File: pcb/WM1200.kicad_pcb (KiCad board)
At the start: 4 copper layers, 159 x 104 mm, 133 parts, among them Q1 BC817, Q2 BC817, Q3 BC817, Q4 BC817, Q5 BC817, Q6 BC817, U1 74LVCH162245A, U2 74LVCH162245A, U3 74LVCH162245A, U4 74LVCH162245A, U5 74LVCH162245A, U6 ADP2108AUJ-3.3, U7 TPD12S016PWR, X1 audio_expansion, X2 A1200_trapdoor_connector, X4 AC7020, X5 Conn_02x05_Odd_Even, X6 HDMI_A

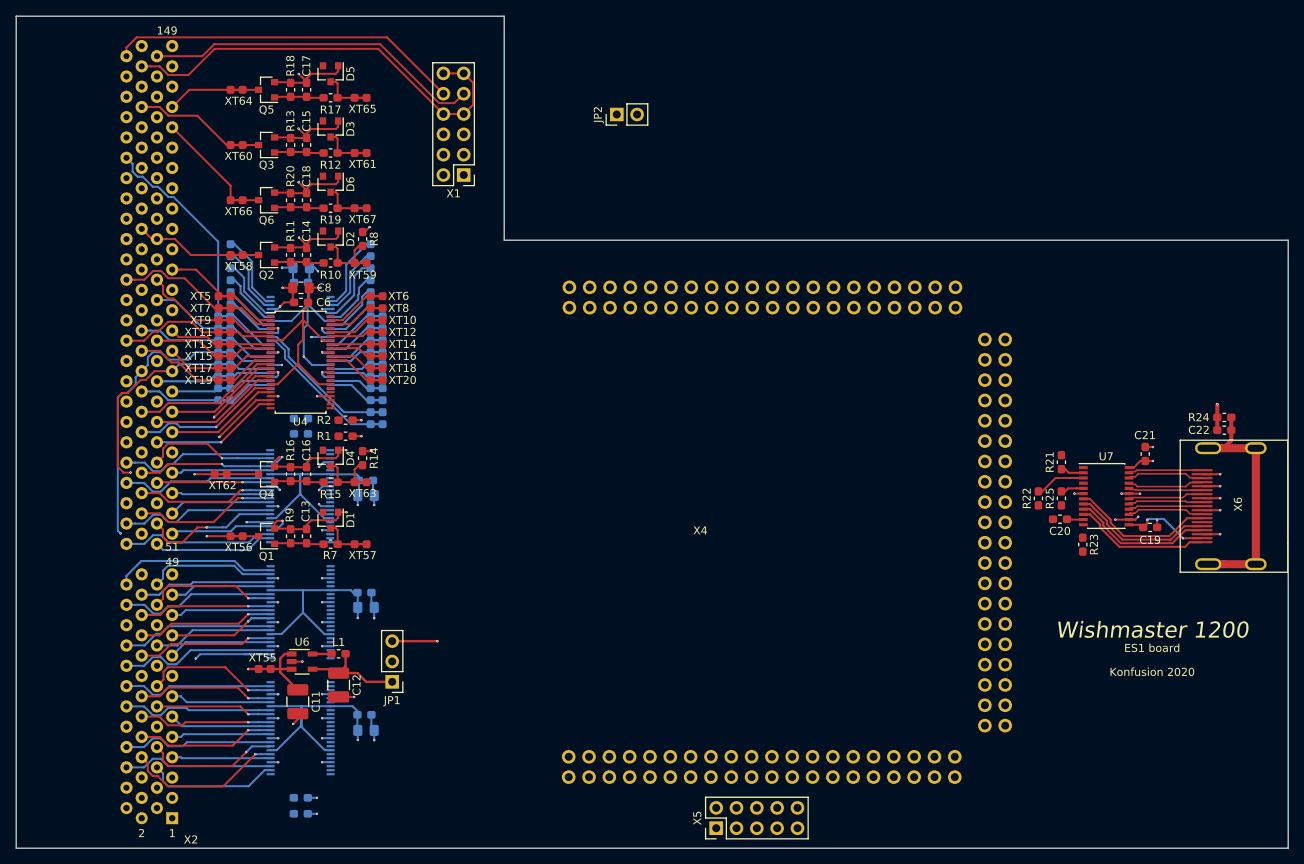
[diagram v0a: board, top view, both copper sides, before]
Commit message: Buffers power scheme rework in progress, re-annotate board
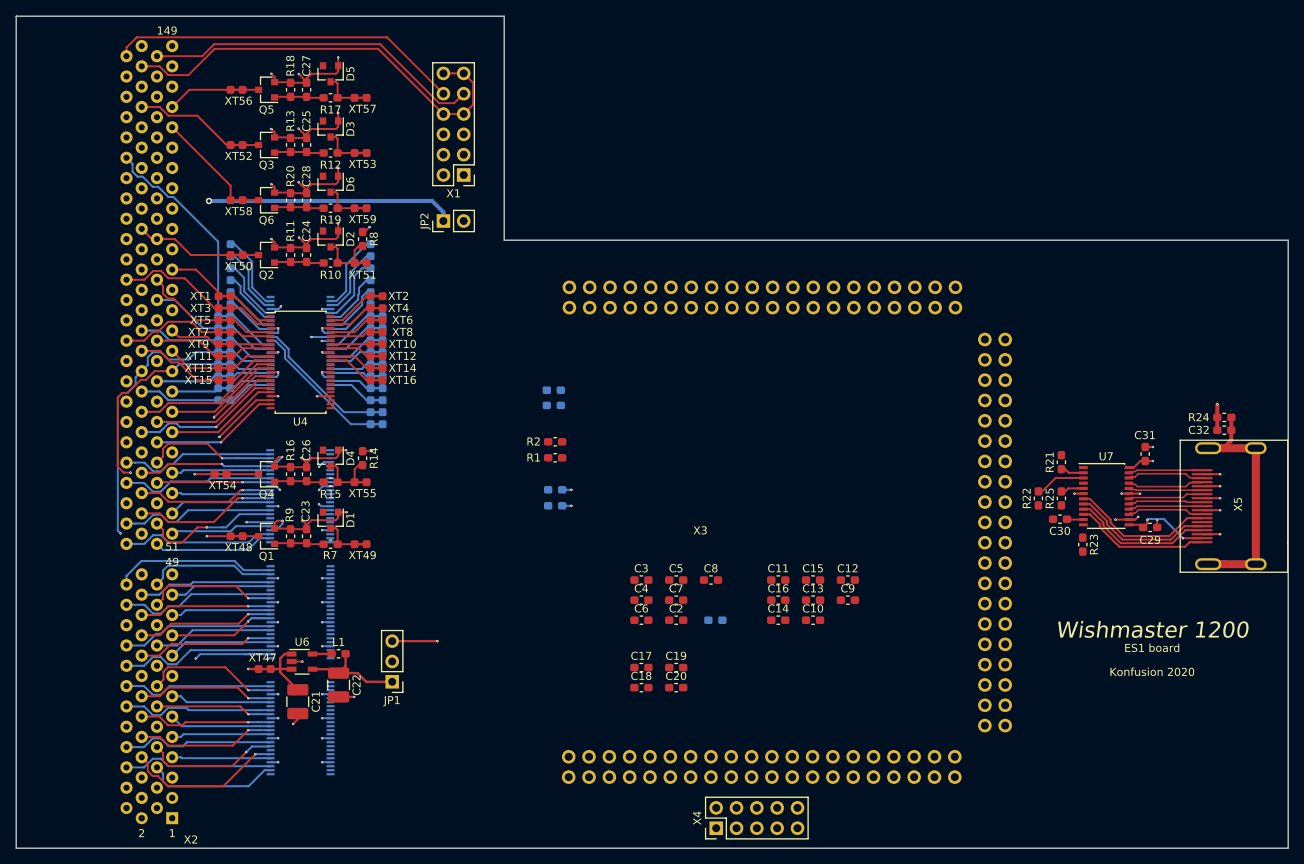
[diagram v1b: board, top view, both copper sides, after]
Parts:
- added C11: 0.1uF 35V, Capacitor_SMD:C_0603_1608Metric_Pad1.05x0.95mm_HandSolder, F.Cu at (185.3, 116.5)
- added C12: 0.1uF 35V, Capacitor_SMD:C_0603_1608Metric_Pad1.05x0.95mm_HandSolder, F.Cu at (194.0, 116.5)
- added C13: 0.1uF 35V, Capacitor_SMD:C_0603_1608Metric_Pad1.05x0.95mm_HandSolder, F.Cu at (189.6, 119.0)
- added C14: 0.1uF 35V, Capacitor_SMD:C_0603_1608Metric_Pad1.05x0.95mm_HandSolder, F.Cu at (185.3, 121.5)
- added C15: 0.1uF 35V, Capacitor_SMD:C_0603_1608Metric_Pad1.05x0.95mm_HandSolder, F.Cu at (189.6, 116.5)
- added C16: 0.1uF 35V, Capacitor_SMD:C_0603_1608Metric_Pad1.05x0.95mm_HandSolder, F.Cu at (185.3, 119.0)
- added C17: 0.1uF 35V, Capacitor_SMD:C_0603_1608Metric_Pad1.05x0.95mm_HandSolder, F.Cu at (168.2, 127.4)
- added C18: 0.1uF 35V, Capacitor_SMD:C_0603_1608Metric_Pad1.05x0.95mm_HandSolder, F.Cu at (168.2, 129.9)
- added C19: 0.1uF 35V, Capacitor_SMD:C_0603_1608Metric_Pad1.05x0.95mm_HandSolder, F.Cu at (172.5, 127.4)
- added C20: 0.1uF 35V, Capacitor_SMD:C_0603_1608Metric_Pad1.05x0.95mm_HandSolder, F.Cu at (172.5, 129.9)
- C10, C3, C4, C7: value 1uF 35V -> 0.1uF 35V; footprint Capacitor_SMD:C_0805_2012Metric_Pad1.15x1.40mm_HandSolder -> Capacitor_SMD:C_0603_1608Metric_Pad1.05x0.95mm_HandSolder; moved to F.Cu
- C2, C5, C9: moved to F.Cu
- C8: value 1uF 35V -> 0.1uF 35V; footprint Capacitor_SMD:C_0805_2012Metric_Pad1.15x1.40mm_HandSolder -> Capacitor_SMD:C_0603_1608Metric_Pad1.05x0.95mm_HandSolder
- moved C9 79.1 mm to (194.0, 119.0)
- moved C10 77.7 mm to (189.6, 121.5)
- moved C8 62.9 mm to (176.8, 116.5)
- moved C6 58.2 mm to (168.2, 121.5)
- moved R3 49.9 mm to (157.4, 105.2)
- moved R4 49.9 mm to (157.4, 107.2)
- moved C1 44.0 mm to (177.4, 121.5)
- moved C2 42.5 mm to (172.5, 121.5), turned to 0 degrees
- moved C5 42.5 mm to (172.5, 116.5), turned to 0 degrees
- moved C7 42.1 mm to (172.5, 119.0), turned to 0 degrees
- moved C4 36.8 mm to (168.2, 119.0), turned to 0 degrees
- moved C3 34.6 mm to (168.2, 116.5), turned to 0 degrees
- moved R5 31.8 mm to (157.2, 92.8)
- moved R6 31.8 mm to (157.2, 94.7)
- moved R1 26.3 mm to (157.4, 101.2)
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- renumbered C11 to C21, C12 to C22, C13 to C23, C14 to C24, C15 to C25, C16 to C26, C17 to C27, C18 to C28, C19 to C29, C20 to C30, C21 to C31, C22 to C32, X4 to X3, X5 to X4, X6 to X5, XT5 to XT1, XT14 to XT10, XT15 to XT11, XT16 to XT12, XT17 to XT13, XT18 to XT14, XT19 to XT15, XT20 to XT16, XT37 to XT17, XT38 to XT18, XT39 to XT19, XT6 to XT2, XT40 to XT20, XT41 to XT21, XT42 to XT22, XT43 to XT23, XT44 to XT24, XT45 to XT25, XT46 to XT26, XT47 to XT27, XT48 to XT28, XT49 to XT29, XT7 to XT3, XT50 to XT30, XT51 to XT31, XT52 to XT32, XT21 to XT33, XT23 to XT34, XT24 to XT35, XT26 to XT36, XT27 to XT37, XT28 to XT38, XT29 to XT39, XT8 to XT4, XT30 to XT40, XT31 to XT41, XT32 to XT42, XT33 to XT43, XT34 to XT44, XT35 to XT45, XT36 to XT46, XT55 to XT47, XT56 to XT48, XT57 to XT49, XT9 to XT5, XT58 to XT50, XT59 to XT51, XT60 to XT52, XT61 to XT53, XT62 to XT54, XT63 to XT55, XT64 to XT56, XT65 to XT57, XT66 to XT58, XT67 to XT59, XT10 to XT6, XT11 to XT7, XT12 to XT8, XT13 to XT9
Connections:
- X3 pad J10_26: FPGA_A_BUFF_DIR -> Net-(X3-PadJ10_26)
- X3 pad J10_28: _FPGA_A_BUFF_OE -> Net-(X3-PadJ10_28)
- X3 pad J12_34: FPGA_D_BUFF_DIR -> Net-(X3-PadJ12_34)
- X3 pad J12_36: _FPGA_D_BUFF_OE -> Net-(X3-PadJ12_36)
- XT33 pad 1: _FPGA_DSACK1 -> Net-(XT33-Pad1)
- XT34 pad 1: _FPGA_DSACK0 -> Net-(XT34-Pad1)
- XT49 pad 1: FPGA_OC_HLT -> Net-(XT49-Pad1)
- XT51 pad 1: FPGA_OC_BOSS -> Net-(XT51-Pad1)
- XT53 pad 1: FPGA_OC_INT6 -> Net-(XT53-Pad1)
- XT55 pad 1: FPGA_OC_RST -> Net-(XT55-Pad1)
- XT57 pad 1: FPGA_OC_INT2 -> Net-(XT57-Pad1)
- XT59 pad 1: FPGA_OC_OVR -> Net-(XT59-Pad1)
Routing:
- net +3V3_BUFFER: track 151.7 -> 3.46 mm, vias 11 -> 3
- net +5VDC: track 5.12 -> 36.1 mm, vias 1 -> 2
- net GND: track 164.9 -> 156.3 mm, vias 63 -> 67

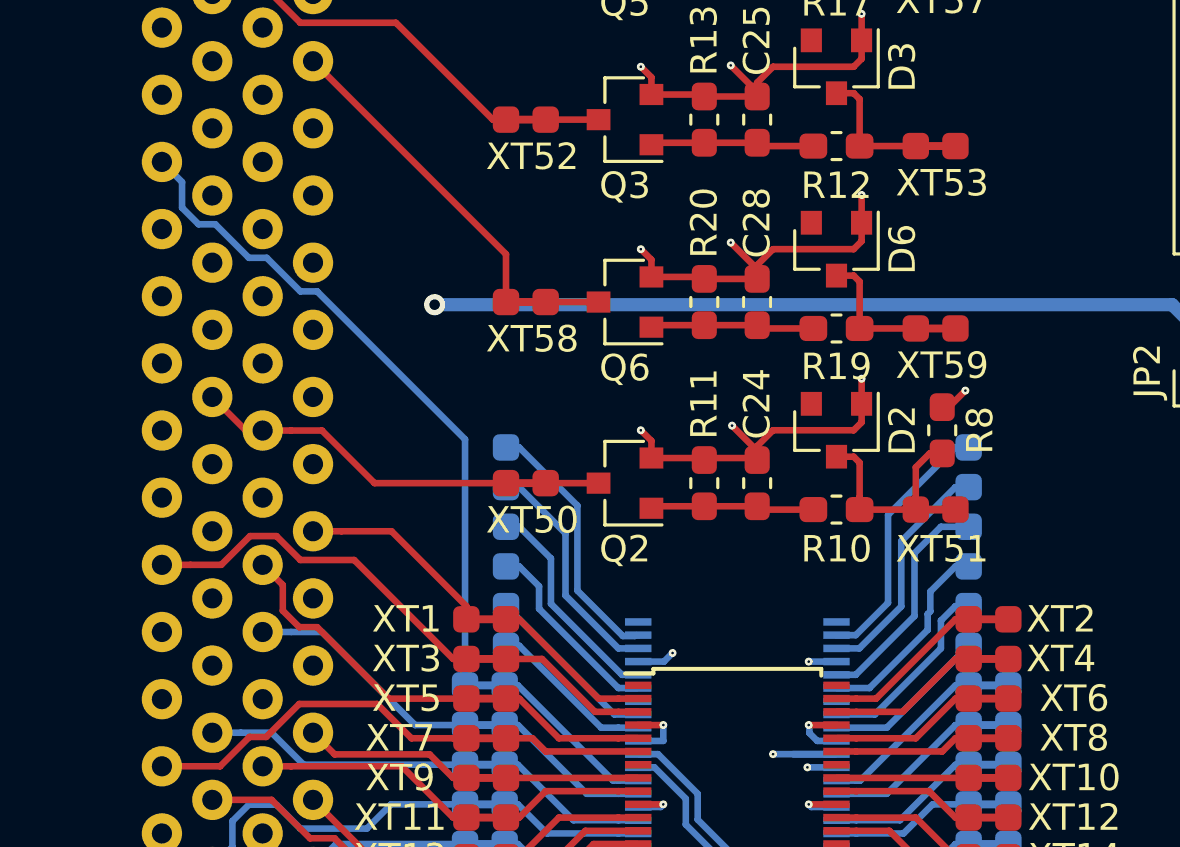
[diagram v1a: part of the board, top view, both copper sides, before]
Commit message: Unused buffer io are now grounded via testpads
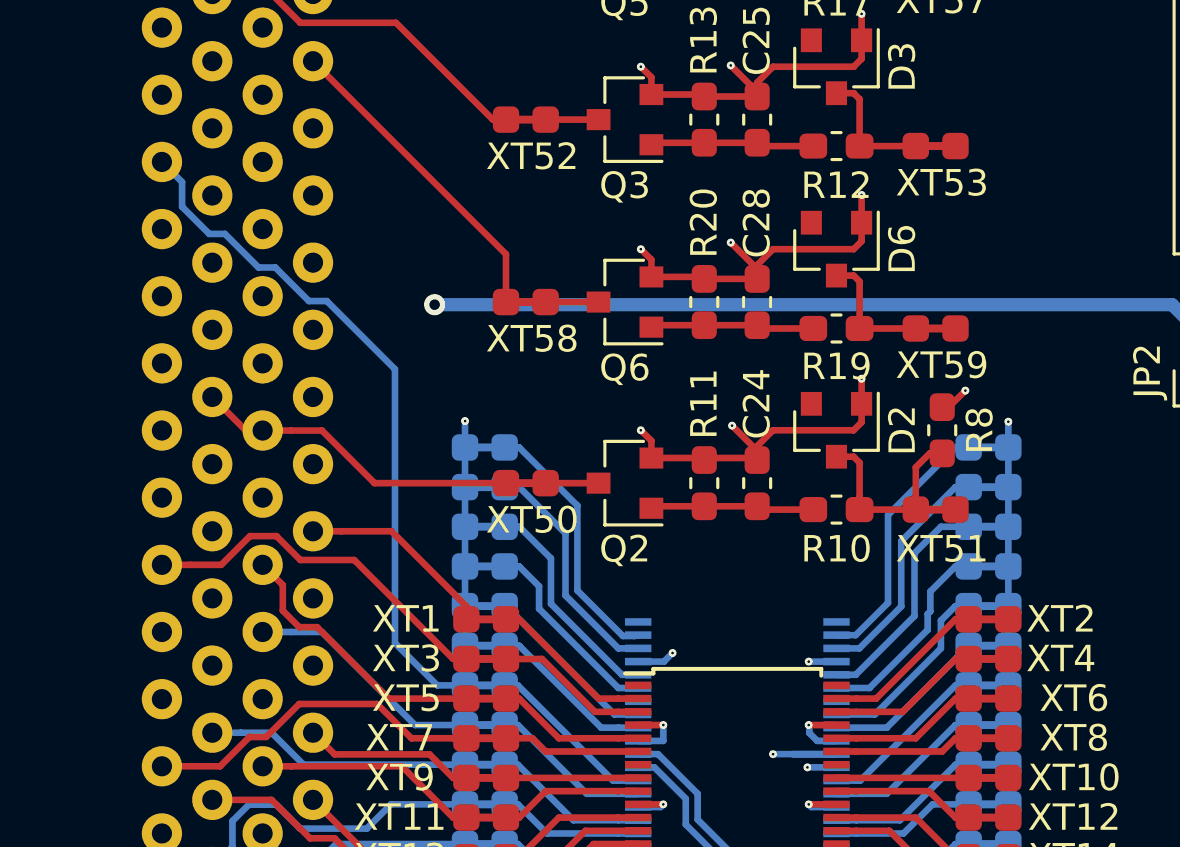
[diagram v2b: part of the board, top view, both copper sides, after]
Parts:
- XT35, XT36, XT37, XT38, XT39, XT40, XT41, XT42, XT43, XT44, XT45, XT46: value testpoint -> testpoint_cutline; footprint WM1200:testpoint -> WM1200:testpoint_cutline
- moved XT37 18.6 mm to (115.8, 82.4)
- moved XT39 18.6 mm to (115.8, 80.9)
- moved XT41 18.6 mm to (115.8, 79.4)
- moved XT43 18.6 mm to (115.8, 77.9)
- moved XT45 18.6 mm to (115.8, 76.4)
- moved XT36 18.3 mm to (134.8, 83.9)
- moved XT38 18.3 mm to (134.8, 82.4)
- moved XT40 18.3 mm to (134.8, 80.9)
- moved XT42 18.3 mm to (134.8, 79.4)
- moved XT44 18.3 mm to (134.8, 77.9), turned to 0 degrees
- moved XT35 2.18 mm to (115.8, 83.9)
- moved XT46 1.97 mm to (134.8, 76.4)
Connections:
- XT35 pad 1: Net-(U5-Pad16) -> GND
- XT36 pad 1: Net-(U5-Pad17) -> Net-(U5-Pad33)
- XT37 pad 1: Net-(U5-Pad33) -> GND
- XT38 pad 1: Net-(U5-Pad19) -> Net-(U5-Pad32)
- XT39 pad 1: Net-(U5-Pad32) -> GND
- XT40 pad 1: Net-(U5-Pad20) -> Net-(U5-Pad30)
- XT41 pad 1: Net-(U5-Pad30) -> GND
- XT42 pad 1: Net-(U5-Pad22) -> Net-(U5-Pad29)
- XT43 pad 1: Net-(U5-Pad29) -> GND
- XT44 pad 1: Net-(U5-Pad23) -> Net-(U5-Pad27)
- XT45 pad 1: Net-(U5-Pad27) -> GND
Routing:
- net GND: track 156.3 -> 173.3 mm, vias 67 -> 69
- net _KBRESET: track 25.7 -> 26.3 mm

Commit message: Some work done, sync
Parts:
- C1, C10, C11, C12, C13, C14, C15, C16, C2, C3, C4, C5, C6, C7, C8, C9: footprint Capacitor_SMD:C_0603_1608Metric_Pad1.05x0.95mm_HandSolder -> Capacitor_SMD:C_0402_1005Metric
- C17, C18, C19, C20: footprint Capacitor_SMD:C_0603_1608Metric_Pad1.05x0.95mm_HandSolder -> Capacitor_SMD:C_0402_1005Metric; moved to B.Cu
- moved C10 78.7 mm to (119.1, 86.6)
- moved C14 69.3 mm to (120.5, 96.7)
- moved C12 69.1 mm to (131.7, 86.6), turned to 180 degrees
- moved C18 67.2 mm to (119.7, 83.4), turned to 315 degrees
- moved C20 67.0 mm to (119.2, 89.2)
- moved C16 57.9 mm to (132.6, 94.9)
- moved C17 57.3 mm to (131.5, 83.4), turned to 225 degrees
- moved C19 55.5 mm to (131.6, 89.8), turned to 180 degrees
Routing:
- net +3V3_BUFFER: track 3.46 -> 11.5 mm
- net GND: track 173.3 -> 177.0 mm, vias 69 -> 73
- net Net-(U5-Pad17): track 6.70 -> 7.76 mm
- net Net-(U5-Pad16): track 6.28 -> 6.84 mm

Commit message: still working
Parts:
- C11, C13, C15, C2, C3, C4, C5, C6, C7, C8, C9: moved to B.Cu
- XT47: footprint WM1200:testpoint_cutline -> WM1200:testpoint_cutline_fat
- moved C15 73.6 mm to (119.2, 138.0)
- moved C11 67.6 mm to (119.4, 132.0)
- moved C9 63.7 mm to (131.7, 132.2), turned to 180 degrees
- moved C13 60.9 mm to (131.7, 137.8), turned to 180 degrees
- moved C8 57.9 mm to (119.4, 109.0)
- moved C7 53.3 mm to (119.4, 123.5)
- moved C4 51.2 mm to (119.4, 103.2)
- moved C3 48.7 mm to (119.4, 118.0)
- moved C1 45.9 mm to (131.7, 117.8)
- moved C2 44.7 mm to (131.7, 103.2), turned to 180 degrees
- moved C5 41.4 mm to (131.7, 123.2), turned to 180 degrees
- moved C6 38.6 mm to (131.7, 108.8), turned to 180 degrees
- moved C14 3.71 mm to (119.5, 93.1), turned to 45 degrees
- moved JP2 3.12 mm to (143.4, 74.7)
- moved C16 2.66 mm to (131.2, 92.6), turned to 135 degrees
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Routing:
- net +3V3_BUFFER: track 11.5 -> 66.3 mm, vias 3 -> 23
- net GND: track 177.0 -> 190.2 mm, vias 73 -> 89
- net Net-(U4-Pad35): track 0.00 -> 11.8 mm
- net Net-(U4-Pad36): track 0.00 -> 11.7 mm
- net Net-(U4-Pad32): track 0.00 -> 11.6 mm
- net Net-(U4-Pad33): track 0.00 -> 11.5 mm
- net Net-(U4-Pad30): track 0.00 -> 11.4 mm
- net Net-(U4-Pad29): track 0.00 -> 11.3 mm
- net Net-(U4-Pad27): track 0.00 -> 11.0 mm
- net Net-(U4-Pad26): track 0.00 -> 10.8 mm
- net +5VDC: track 36.1 -> 39.2 mm
- net A19: track 16.7 -> 18.8 mm
- net FPGA_VCC3V3: track 8.97 -> 10.2 mm
- net D2: track 22.5 -> 21.3 mm
- net +3V3_DC_DC: track 13.4 -> 12.7 mm

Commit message: some dirty routing
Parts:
- moved X4 50.6 mm to (227.3, 138.7)
- moved R2 37.8 mm to (125.7, 119.7), turned to 0 degrees
- moved R5 35.8 mm to (121.5, 96.0)
- moved R6 35.8 mm to (121.5, 97.9)
- moved R1 35.8 mm to (125.7, 117.7), turned to 0 degrees
- moved R4 33.8 mm to (125.5, 95.9), turned to 0 degrees
- moved R3 32.7 mm to (125.5, 97.9), turned to 0 degrees
- moved JP1 20.6 mm to (123.0, 144.9)
- moved X3 2.10 mm to (137.9, 142.6)
- moved R21 1.17 mm to (219.8, 102.6), turned to 180 degrees
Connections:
- U1 pad 26: Net-(U1-Pad26) -> FPGA_D24
- U1 pad 27: Net-(U1-Pad27) -> FPGA_D25
- U1 pad 29: Net-(U1-Pad29) -> FPGA_D26
- U1 pad 30: Net-(U1-Pad30) -> FPGA_D27
- U1 pad 32: Net-(U1-Pad32) -> FPGA_D28
- U1 pad 33: Net-(U1-Pad33) -> FPGA_D29
- U1 pad 35: Net-(U1-Pad35) -> FPGA_D30
- U1 pad 36: Net-(U1-Pad36) -> FPGA_D31
- U1 pad 37: Net-(U1-Pad37) -> FPGA_A0
- U1 pad 38: Net-(U1-Pad38) -> FPGA_A1
- U1 pad 40: Net-(U1-Pad40) -> FPGA_A2
- U1 pad 41: Net-(U1-Pad41) -> FPGA_A3
- U1 pad 43: Net-(U1-Pad43) -> FPGA_A4
- U1 pad 44: Net-(U1-Pad44) -> FPGA_A5
- U1 pad 46: Net-(U1-Pad46) -> FPGA_A6
- U1 pad 47: Net-(U1-Pad47) -> FPGA_A7
- U2 pad 26: Net-(U2-Pad26) -> FPGA_D8
- U2 pad 27: Net-(U2-Pad27) -> FPGA_D9
- U2 pad 29: Net-(U2-Pad29) -> FPGA_D10
- U2 pad 30: Net-(U2-Pad30) -> FPGA_D11
- U2 pad 32: Net-(U2-Pad32) -> FPGA_D12
- U2 pad 33: Net-(U2-Pad33) -> FPGA_D13
- U2 pad 35: Net-(U2-Pad35) -> FPGA_D14
- U2 pad 36: Net-(U2-Pad36) -> FPGA_D15
- U2 pad 37: Net-(U2-Pad37) -> FPGA_D16
- U2 pad 38: Net-(U2-Pad38) -> FPGA_D17
- U2 pad 40: Net-(U2-Pad40) -> FPGA_D18
- U2 pad 41: Net-(U2-Pad41) -> FPGA_D19
- U2 pad 43: Net-(U2-Pad43) -> FPGA_D20
- U2 pad 44: Net-(U2-Pad44) -> FPGA_D21
- U2 pad 46: Net-(U2-Pad46) -> FPGA_D22
- U2 pad 47: Net-(U2-Pad47) -> FPGA_D23
- U3 pad 26: Net-(U3-Pad26) -> FPGA_A8
- U3 pad 27: Net-(U3-Pad27) -> FPGA_A9
- U3 pad 29: Net-(U3-Pad29) -> FPGA_A10
- U3 pad 30: Net-(U3-Pad30) -> FPGA_A11
- U3 pad 32: Net-(U3-Pad32) -> FPGA_A12
- U3 pad 33: Net-(U3-Pad33) -> FPGA_A13
- U3 pad 35: Net-(U3-Pad35) -> FPGA_A14
- U3 pad 36: Net-(U3-Pad36) -> FPGA_A15
- U3 pad 37: Net-(U3-Pad37) -> FPGA_A16
- U3 pad 38: Net-(U3-Pad38) -> FPGA_A17
- U3 pad 40: Net-(U3-Pad40) -> FPGA_A18
- U3 pad 41: Net-(U3-Pad41) -> FPGA_A19
- U3 pad 43: Net-(U3-Pad43) -> FPGA_A20
- U3 pad 44: Net-(U3-Pad44) -> FPGA_A21
- U3 pad 46: Net-(U3-Pad46) -> FPGA_A22
- U3 pad 47: Net-(U3-Pad47) -> FPGA_A23
- U4 pad 26: Net-(U4-Pad26) -> FPGA_D7
- U4 pad 27: Net-(U4-Pad27) -> FPGA_D6
- U4 pad 29: Net-(U4-Pad29) -> FPGA_D5
- U4 pad 30: Net-(U4-Pad30) -> FPGA_D4
- U4 pad 32: Net-(U4-Pad32) -> FPGA_D3
- U4 pad 33: Net-(U4-Pad33) -> FPGA_D2
- U4 pad 35: Net-(U4-Pad35) -> FPGA_D1
- U4 pad 36: Net-(U4-Pad36) -> FPGA_D0
- X3 pad J10_10: FPGA_A16 -> FPGA_A20
- X3 pad J10_12: FPGA_A17 -> FPGA_A19
- X3 pad J10_16: FPGA_A19 -> FPGA_A17
- X3 pad J10_18: FPGA_A20 -> FPGA_A16
- X3 pad J10_20: FPGA_A21 -> FPGA_A15
- X3 pad J10_22: FPGA_A22 -> FPGA_A14
- X3 pad J10_24: FPGA_A23 -> FPGA_A13
- X3 pad J10_26: Net-(X3-PadJ10_26) -> FPGA_A12
- X3 pad J10_27: FPGA_A12 -> _FPGA_A_BUFF_OE
- X3 pad J10_28: Net-(X3-PadJ10_28) -> FPGA_A_BUFF_DIR
- X3 pad J10_4: FPGA_A13 -> FPGA_A23
- X3 pad J10_6: FPGA_A14 -> FPGA_A22
- X3 pad J10_8: FPGA_A15 -> FPGA_A21
- X3 pad J12_10: FPGA_D20 -> FPGA_D14
- X3 pad J12_11: FPGA_D4 -> FPGA_D17
- X3 pad J12_12: FPGA_D21 -> FPGA_D16
- X3 pad J12_13: FPGA_D5 -> FPGA_D19
- X3 pad J12_14: FPGA_D22 -> FPGA_D18
- X3 pad J12_15: FPGA_D6 -> FPGA_D21
- X3 pad J12_16: FPGA_D23 -> FPGA_D20
- X3 pad J12_17: FPGA_D7 -> FPGA_D23
- X3 pad J12_18: FPGA_D24 -> FPGA_D22
- X3 pad J12_19: FPGA_D8 -> FPGA_D25
- X3 pad J12_20: FPGA_D25 -> FPGA_D24
- X3 pad J12_21: FPGA_D9 -> FPGA_D27
- X3 pad J12_23: FPGA_D10 -> FPGA_D29
- X3 pad J12_24: FPGA_D27 -> FPGA_D28
- X3 pad J12_25: FPGA_D11 -> FPGA_D31
- X3 pad J12_26: FPGA_D28 -> FPGA_D30
- X3 pad J12_27: FPGA_D12 -> _FPGA_D_BUFF_OE
- X3 pad J12_28: FPGA_D29 -> FPGA_D_BUFF_DIR
- X3 pad J12_29: FPGA_D13 -> FPGA_D1
- X3 pad J12_3: FPGA_D0 -> FPGA_D9
- X3 pad J12_30: FPGA_D30 -> FPGA_D0
- X3 pad J12_31: FPGA_D14 -> FPGA_D3
- X3 pad J12_32: FPGA_D31 -> FPGA_D2
- X3 pad J12_33: FPGA_D15 -> FPGA_D5
- X3 pad J12_34: Net-(X3-PadJ12_34) -> FPGA_D4
- X3 pad J12_35: FPGA_D16 -> FPGA_D7
- X3 pad J12_36: Net-(X3-PadJ12_36) -> FPGA_D6
- X3 pad J12_4: FPGA_D17 -> FPGA_D8
- X3 pad J12_5: FPGA_D1 -> FPGA_D11
- X3 pad J12_6: FPGA_D18 -> FPGA_D10
- X3 pad J12_7: FPGA_D2 -> FPGA_D13
- X3 pad J12_8: FPGA_D19 -> FPGA_D12
- X3 pad J12_9: FPGA_D3 -> FPGA_D15
- X4 pad 1: FPGA_PS_MIO10 -> FPGA_PS_MIO14
- X4 pad 2: FPGA_PS_MIO11 -> FPGA_PS_MIO9
- X4 pad 3: FPGA_PS_MIO12 -> FPGA_PS_MIO13
- X4 pad 4: FPGA_PS_MIO13 -> FPGA_PS_MIO11
- X4 pad 5: FPGA_PS_MIO14 -> FPGA_PS_MIO10
- X4 pad 7: FPGA_PS_MIO9 -> FPGA_PS_MIO12
- XT10 pad 2: Net-(XT10-Pad2) -> FPGA_R_W
- XT12 pad 2: Net-(XT12-Pad2) -> _FPGA_AS
- XT14 pad 2: Net-(XT14-Pad2) -> FPGA_SIZE1
- XT16 pad 2: Net-(XT16-Pad2) -> FPGA_SIZE0
- XT18 pad 2: Net-(XT18-Pad2) -> _FPGA_IPL1
- XT2 pad 2: Net-(XT2-Pad2) -> FPGA_FC0
- XT20 pad 2: Net-(XT20-Pad2) -> _FPGA_IPL2
- XT22 pad 2: Net-(XT22-Pad2) -> _FPGA_IPL0
- XT24 pad 2: Net-(XT24-Pad2) -> _FPGA_RST
- XT26 pad 2: Net-(XT26-Pad2) -> _FPGA_HLT
- XT28 pad 2: Net-(XT28-Pad2) -> _FPGA_BERR
- XT30 pad 2: Net-(XT30-Pad2) -> FPGA_CPUCLK_A
- XT32 pad 2: Net-(XT32-Pad2) -> _FPGA_KBRESET
- XT33 pad 1: Net-(XT33-Pad1) -> _FPGA_DSACK1
- XT34 pad 1: Net-(XT34-Pad1) -> _FPGA_DSACK0
- XT4 pad 2: Net-(XT4-Pad2) -> FPGA_FC1
- XT6 pad 2: Net-(XT6-Pad2) -> FPGA_FC2
- XT8 pad 2: Net-(XT8-Pad2) -> _FPGA_DS
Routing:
- net _FPGA_A_BUFF_OE: track 0.00 -> 171.9 mm, vias 0 -> 4
- net FPGA_A_BUFF_DIR: track 0.00 -> 170.4 mm, vias 0 -> 3
- net FPGA_D_BUFF_DIR: track 0.00 -> 113.8 mm, vias 0 -> 3
- net _FPGA_D_BUFF_OE: track 0.00 -> 112.0 mm, vias 0 -> 3
- net FPGA_PS_MIO12: track 0.00 -> 81.3 mm
- net FPGA_PS_MIO10: track 0.00 -> 81.2 mm
- net FPGA_A0: track 0.00 -> 80.8 mm
- net FPGA_A23: track 0.00 -> 80.4 mm
- net FPGA_D6: track 0.00 -> 78.7 mm
- net FPGA_A22: track 0.00 -> 78.5 mm
- net FPGA_PS_MIO15: track 0.00 -> 78.3 mm
- net FPGA_A1: track 0.00 -> 78.1 mm
- net FPGA_D7: track 0.00 -> 77.4 mm
- net FPGA_D4: track 0.00 -> 76.0 mm
- net FPGA_D30: track 0.00 -> 75.7 mm
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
